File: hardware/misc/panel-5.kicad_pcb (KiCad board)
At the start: 2 copper layers, 59 x 24.1 mm, 54 parts, among them J1 Conn_01x02_Male, J2 Conn_01x03, J3 Conn_01x02, J5 Conn_01x02_Male, J6 Conn_01x02_Male, J7 Conn_01x02_Male, U1 A7105-MODULE, U2 AIC1734-33GUTR, U3 ATtiny1617-M, U5 DRV8837DSGR, U6 DRV8837DSGR, U7 DRV8837DSGR

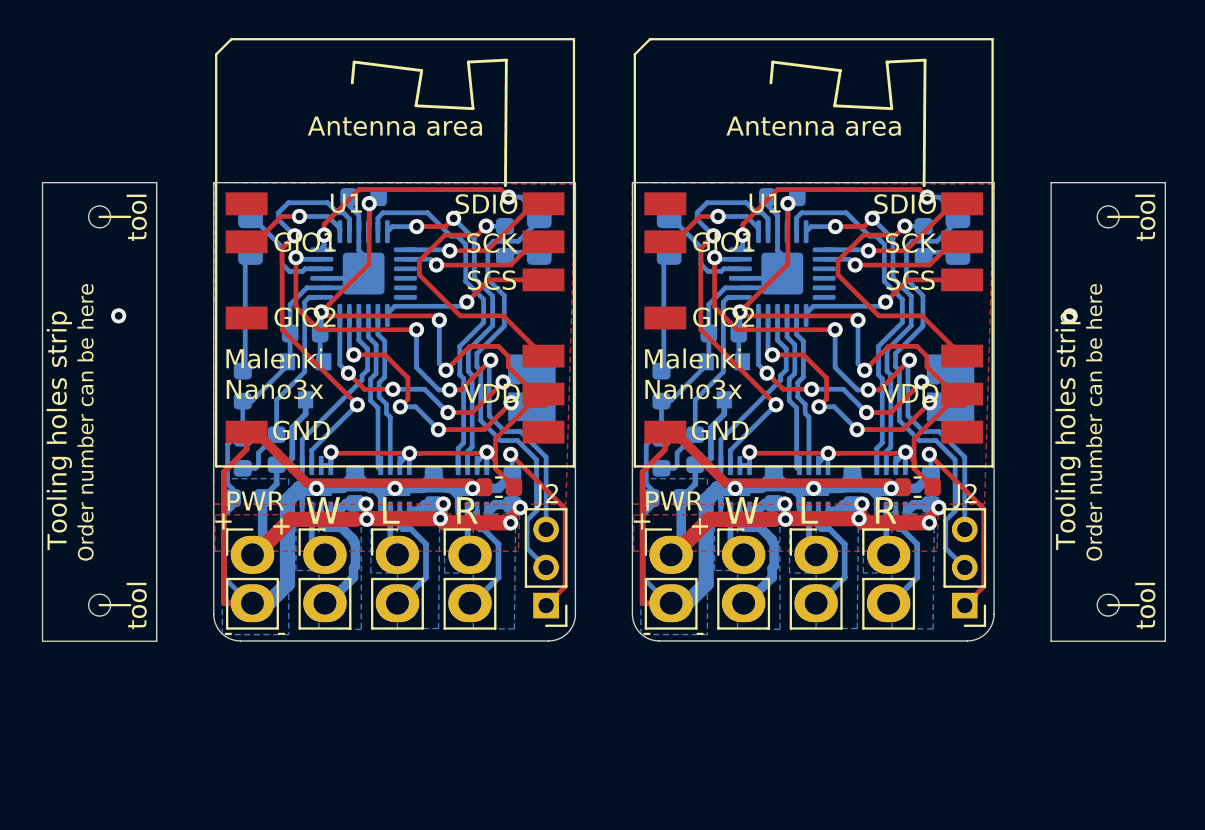
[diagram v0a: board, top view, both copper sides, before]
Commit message: Panelisation changes
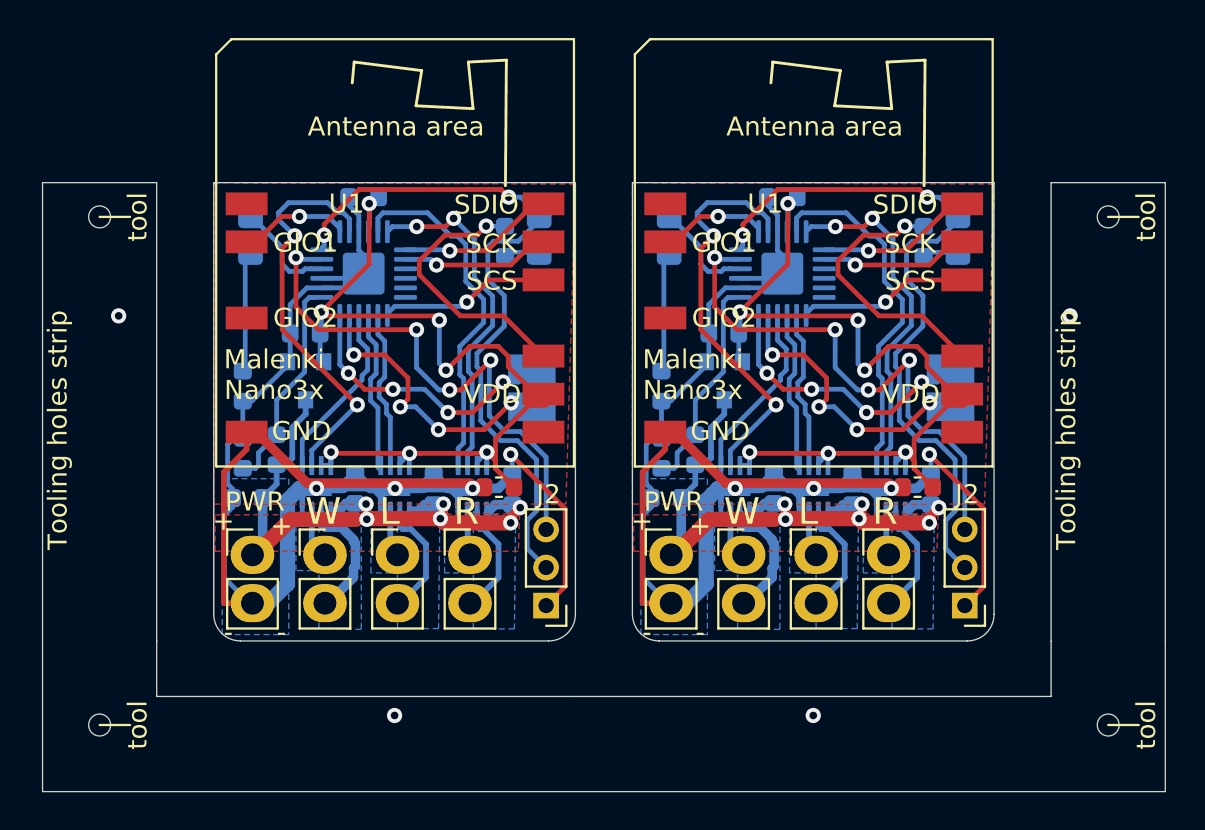
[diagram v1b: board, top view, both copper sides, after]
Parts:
- removed the REF** at (94.0, 72.2)
- removed the REF** at (147.0, 72.2)
- added REF**: toolhole, misc:toolhole, F.Cu at (94.0, 78.5)
- added REF**: toolhole, misc:toolhole, F.Cu at (147.0, 78.5)
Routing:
- net (no net): vias 2 -> 4
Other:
- board size 59 x 24.1 mm -> 59 x 32 mm
- board text removed: "Order number can be here"
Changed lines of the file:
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@@
   (general
     (thickness 1.6)
-    (drawings 71)
-    (tracks 864)
+    (drawings 78)
+    (tracks 866)
     (modules 54)
     (nets 35)
@@
     (pad_to_mask_clearance 0.051)
     (solder_mask_min_width 0.25)
-    (aux_axis_origin 90 75)
+    (aux_axis_origin 90 83)
     (visible_elements FFFDF77F)
     (pcbplotparams
@@
   )
   (module "misc:toolhole" (layer "F.Cu")
-    (at 94 72.2 90)
+    (at 94 78.5 90)
     (fp_text reference "REF**" (at 0 2.54 90 unlocked) (layer "F.SilkS") hide
       (effects (font (size 1 1) (thickness 0.15)))
@@
   )
   (module "misc:toolhole" (layer "F.Cu")
-    (at 147 72.2 90)
+    (at 147 78.5 90)
     (fp_text reference "REF**" (at 0 2.54 90 unlocked) (layer "F.SilkS") hide
       (effects (font (size 1 1) (thickness 0.15)))
@@
       (solder_mask_margin 0.6))
   )
+  (gr_line (start 100 77.5) (end 100 81.5) (layer "Eco2.User") (width 0.1))
+  (gr_line (start 141 77.5) (end 141 81.5) (layer "Eco2.User") (width 0.1))
+  (gr_line (start 131.5 78) (end 131.5 72) (layer "Eco1.User") (width 0.1))
+  (gr_line (start 109.5 78) (end 109.5 72) (layer "Eco1.User") (width 0.1))
+  (gr_line (start 91 82) (end 91 74.1) (layer "Edge.Cuts") (width 0.05))
+  (gr_line (start 150 82) (end 91 82) (layer "Edge.Cuts") (width 0.05))
+  (gr_line (start 150 74.1) (end 150 82) (layer "Edge.Cuts") (width 0.05))
+  (gr_line (start 144 77) (end 144 74.1) (layer "Edge.Cuts") (width 0.05))
+  (gr_line (start 97 77) (end 97 74.1) (layer "Edge.Cuts") (width 0.05))
+  (gr_line (start 119 77) (end 97 77) (layer "Edge.Cuts") (width 0.05))
+  (gr_line (start 144 77) (end 119 77) (layer "Edge.Cuts") (width 0.05))
   (gr_line (start 139 57) (end 145 57) (layer "Eco1.User") (width 0.1))
   (gr_line (start 117 57) (end 123 57) (layer "Eco1.User") (width 0.1))
@@
   (gr_line (start 122 50) (end 121.997182 72.671006) (layer "Edge.Cuts") (width 0.05))
   (gr_line (start 141.002 50) (end 122 50) (layer "Edge.Cuts") (width 0.05))
-  (gr_text "Order number can be here" (at 93.3 62.6 90) (layer "F.SilkS")
-    (effects (font (size 0.8 0.8) (thickness 0.15)))
-  )
   (gr_text "Tooling holes strip" (at 91.8 63 90) (layer "F.SilkS")
     (effects (font (size 1 1) (thickness 0.15)))
   )
-  (gr_line (start 91 74.1) (end 97 74.1) (layer "Edge.Cuts") (width 0.05))
   (gr_line (start 91 50) (end 91 74.1) (layer "Edge.Cuts") (width 0.05))
   (gr_line (start 97 50) (end 97 74.1) (layer "Edge.Cuts") (width 0.05))
   (gr_line (start 91 50) (end 97 50) (layer "Edge.Cuts") (width 0.05))
-  (gr_text "Order number can be here" (at 146.3 62.6 90) (layer "F.SilkS")
-    (effects (font (size 0.8 0.8) (thickness 0.15)))
-  )
   (gr_text "Tooling holes strip" (at 144.8 63 90) (layer "F.SilkS")
     (effects (font (size 1 1) (thickness 0.15)))
   )
-  (gr_line (start 144 74.1) (end 150 74.1) (layer "Edge.Cuts") (width 0.05))
   (gr_line (start 144 50) (end 144 74.1) (layer "Edge.Cuts") (width 0.05))
   (gr_line (start 150 50) (end 150 74.1) (layer "Edge.Cuts") (width 0.05))
@@
   (via (at 95 57) (size 0.8) (drill 0.4) (layers "F.Cu" "B.Cu") (net 0))
   (via (at 145 57) (size 0.8) (drill 0.4) (layers "F.Cu" "B.Cu") (net 0))
+  (via (at 109.5 78) (size 0.8) (drill 0.4) (layers "F.Cu" "B.Cu") (net 0))
+  (via (at 131.5 78) (size 0.8) (drill 0.4) (layers "F.Cu" "B.Cu") (net 0))
   (zone (net 9) (net_name "Net-(J5-Pad1)") (layer "B.Cu") (hatch edge 0.508)
     (connect_pads yes (clearance 0.21))
